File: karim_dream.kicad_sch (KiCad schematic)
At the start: 0 parts

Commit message: start working on microcontroller schematic
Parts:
- added C? (x2): 22pF, symbol Device:C_Small
- added C?: 1u, symbol Device:C_Small
- added R?: 10k, symbol Device:R_Small
- added U?: AT90USB647-A, Package_QFP:TQFP-64_14x14mm_P0.8mm, symbol MCU_Microchip_AVR:AT90USB647-A
- added Y?: 16Mhz, symbol Device:Crystal_Small
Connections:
- new net: R?.2, U?.43 (PE2/~{HWB})
- new net: C?.2, U?.23 (XTAL2), Y?.1
- new net: C?.2, U?.24 (XTAL1), Y?.2
- new net: C?.2, U?.7 (UCAP)
- new net +5V: U?.21 (VCC), U?.3 (UVCC), U?.52 (VCC), U?.64 (AVCC), U?.8 (VBUS)
- new net GND: C?.1, C?.1, C?.1, R?.1, U?.22 (GND), U?.53 (GND), U?.6 (UGND), U?.63 (GND)

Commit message: schematic minimum microcontroller setup
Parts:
- added C?: 100n, symbol Device:C_Small
- added R?: 10k, symbol Device:R_Small
- added SW?: SW_Push, symbol Switch:SW_Push
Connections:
- net +5V: now also R?.2
- net GND: now also C?.1, SW?.1
- net RESET: now reaches U?.20 (~{RESET})
- net RESET: now also C?.2, R?.1, SW?.2
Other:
- moved on the sheet: C?, R?, U?, Y?

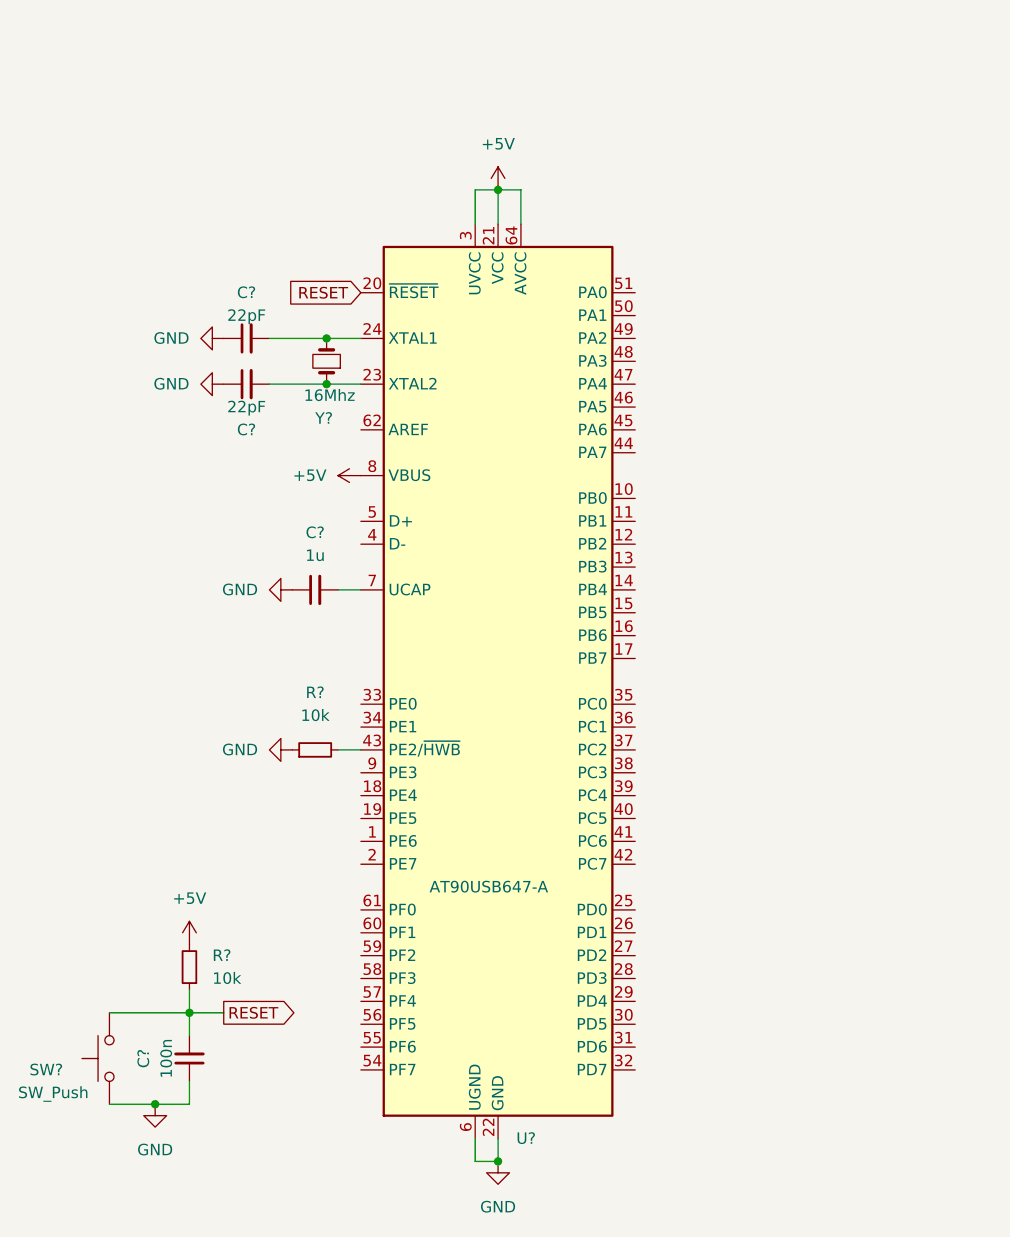
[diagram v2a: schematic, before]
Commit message: add usb to schematic
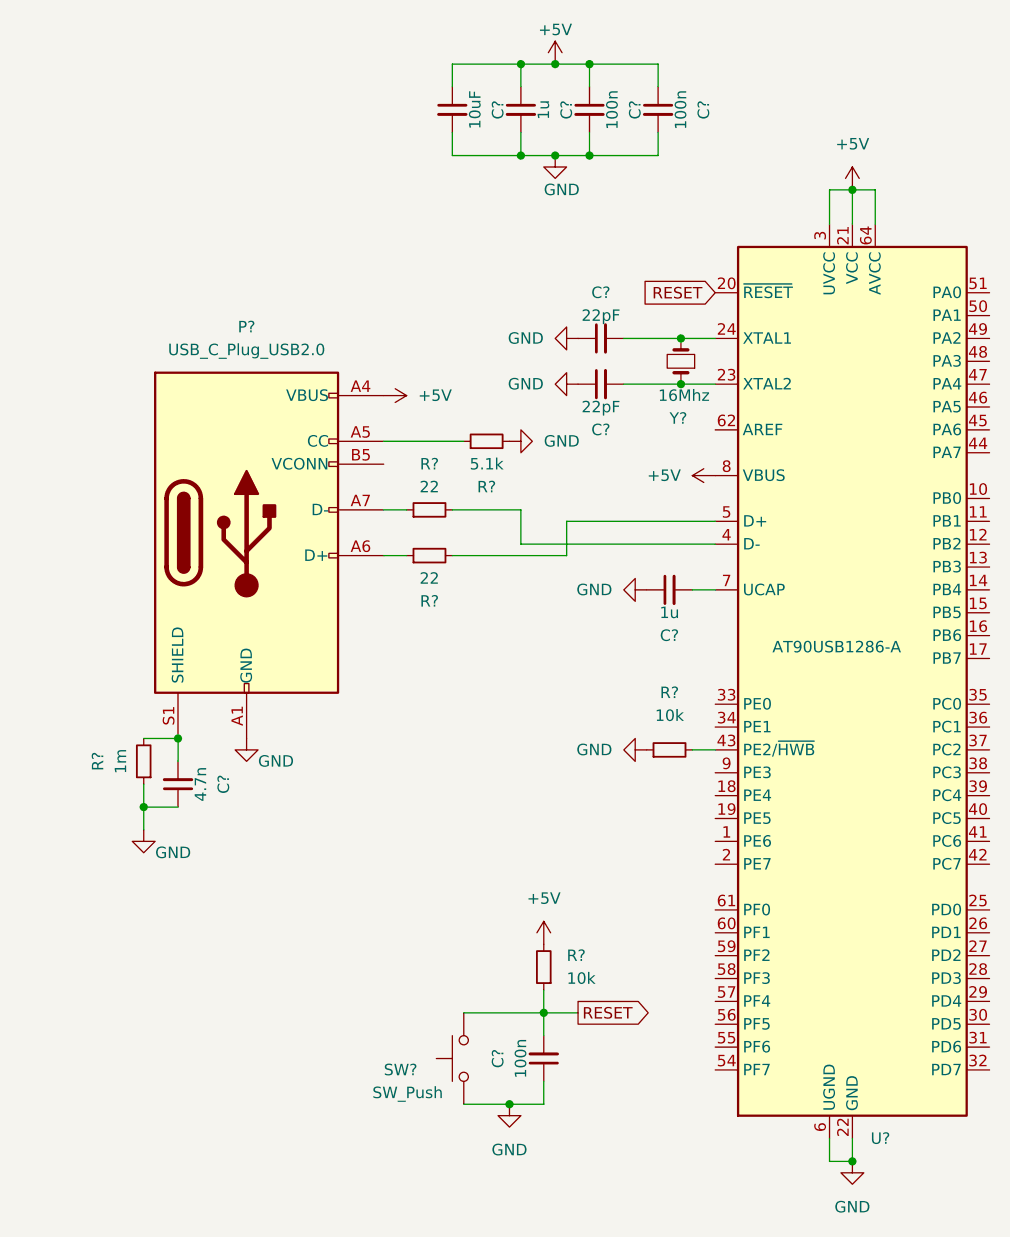
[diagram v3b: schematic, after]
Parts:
- removed U?: AT90USB647-A, Package_QFP:TQFP-64_14x14mm_P0.8mm, symbol MCU_Microchip_AVR:AT90USB647-A
- added C?: 1u, symbol Device:C_Small
- added C? (x2): 100n, symbol Device:C_Small
- added C?: 10uF, symbol Device:C_Small
- added C?: 4.7n, symbol Device:C_Small
- added P?: USB_C_Plug_USB2.0, symbol Connector:USB_C_Plug_USB2.0
- added R?: 1m, symbol Device:R_Small
- added R?: 5.1k, symbol Device:R_Small
- added R? (x2): 22, symbol Device:R_Small
- added U?: AT90USB1286-A, Package_QFP:TQFP-64_14x14mm_P0.8mm, symbol MCU_Microchip_AVR:AT90USB1286-A
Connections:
- net +5V: now also C?.1, C?.1, C?.1, C?.1, P?.A4 (VBUS), P?.A9 (VBUS), P?.B4 (VBUS), P?.B9 (VBUS), U?.21 (VCC), U?.3 (UVCC), U?.52 (VCC), U?.64 (AVCC), U?.8 (VBUS)
- net GND: now also C?.1, C?.2, C?.2, C?.2, C?.2, P?.A1 (GND), P?.A12 (GND), P?.B1 (GND), P?.B12 (GND), R?.1, R?.2, U?.22 (GND), U?.53 (GND), U?.6 (UGND), U?.63 (GND)
- net RESET: now also U?.20 (~{RESET})
- net at R?.2: now also U?.43 (PE2/~{HWB})
- net at C?.2, Y?.1: now also U?.23 (XTAL2)
- net at C?.2, Y?.2: now also U?.24 (XTAL1)
- net at C?.2: now also U?.7 (UCAP)
- new net: R?.2, U?.4 (D-)
- new net: R?.2, U?.5 (D+)
- new net: P?.A5 (CC), R?.1
- new net: P?.A6 (D+), R?.1
- new net: P?.A7 (D-), R?.1
- new net: C?.2, P?.S1 (SHIELD), R?.2
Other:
- moved on the sheet: C?, R?, SW?, Y?

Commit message: add some buttons
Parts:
- added D1, D2, D3, D4, D5, D6: D, symbol Device:D
- added SW1, SW2, SW3, SW4, SW5, SW6: MXSwitch, symbol acheronSymbols:MXSwitch
- gave numbers to parts that had none: 19
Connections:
- new net: D4.2 (A), SW4.2 (Row)
- new net: D5.2 (A), SW5.2 (Row)
- new net: D3.2 (A), SW3.2 (Row)
- new net: D2.2 (A), SW2.2 (Row)
- new net: D1.2 (A), SW1.2 (Row)
- new net: D6.2 (A), SW6.2 (Row)
- new net Col1: D1.1 (K), D2.1 (K), D3.1 (K)
- new net Col2: D4.1 (K), D5.1 (K), D6.1 (K)
- new net Row1: SW1.1 (Col), SW4.1 (Col)
- new net Row2: SW2.1 (Col), SW5.1 (Col)
- new net Row3: SW3.1 (Col), SW6.1 (Col)
